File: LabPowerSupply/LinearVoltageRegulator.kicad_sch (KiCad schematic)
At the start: 17 parts, among them Q1_LVR1 PJA3404_R1_00001, Q2_LVR1 PJA3404_R1_00001, Q3_LVR1 PJA3404_R1_00001

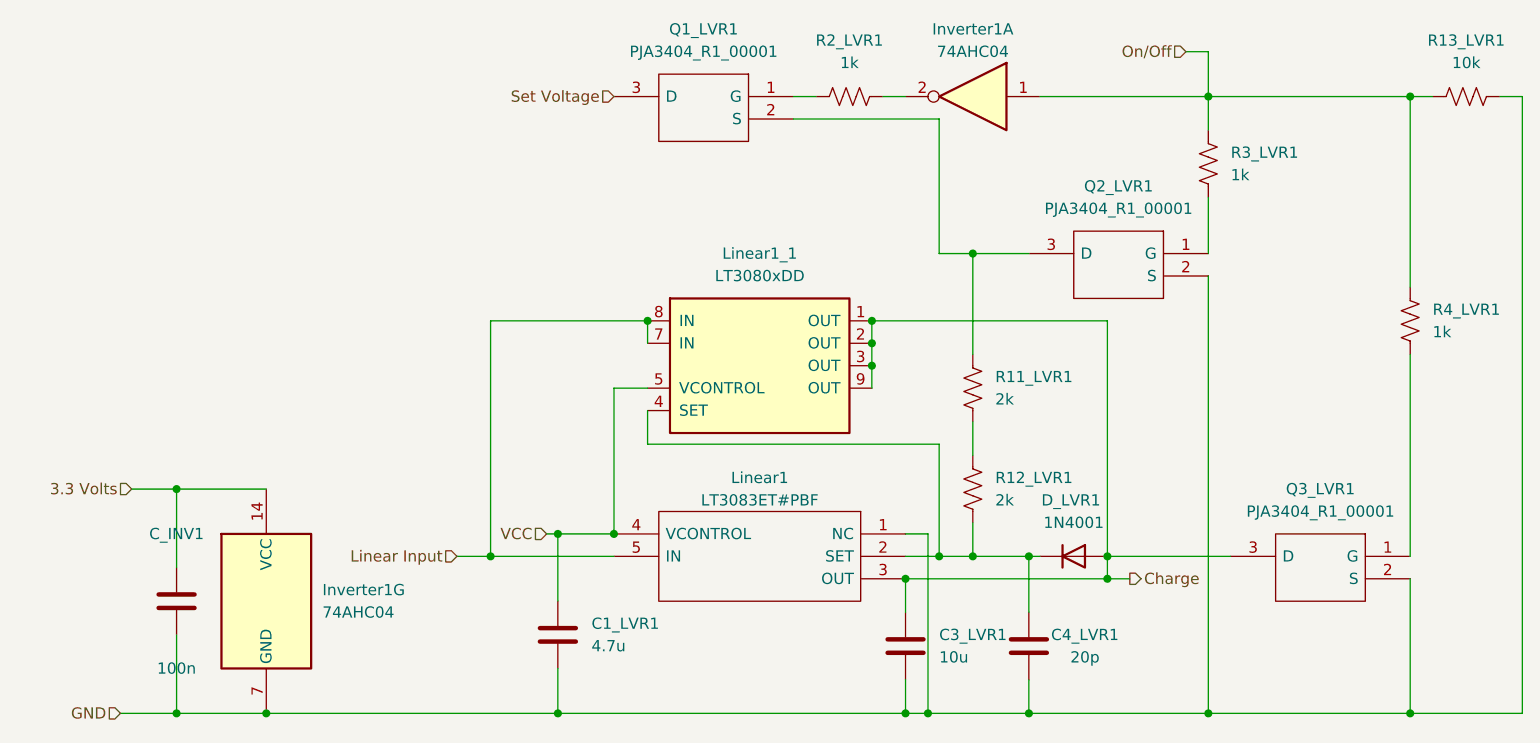
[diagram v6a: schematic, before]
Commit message: Updated Part List
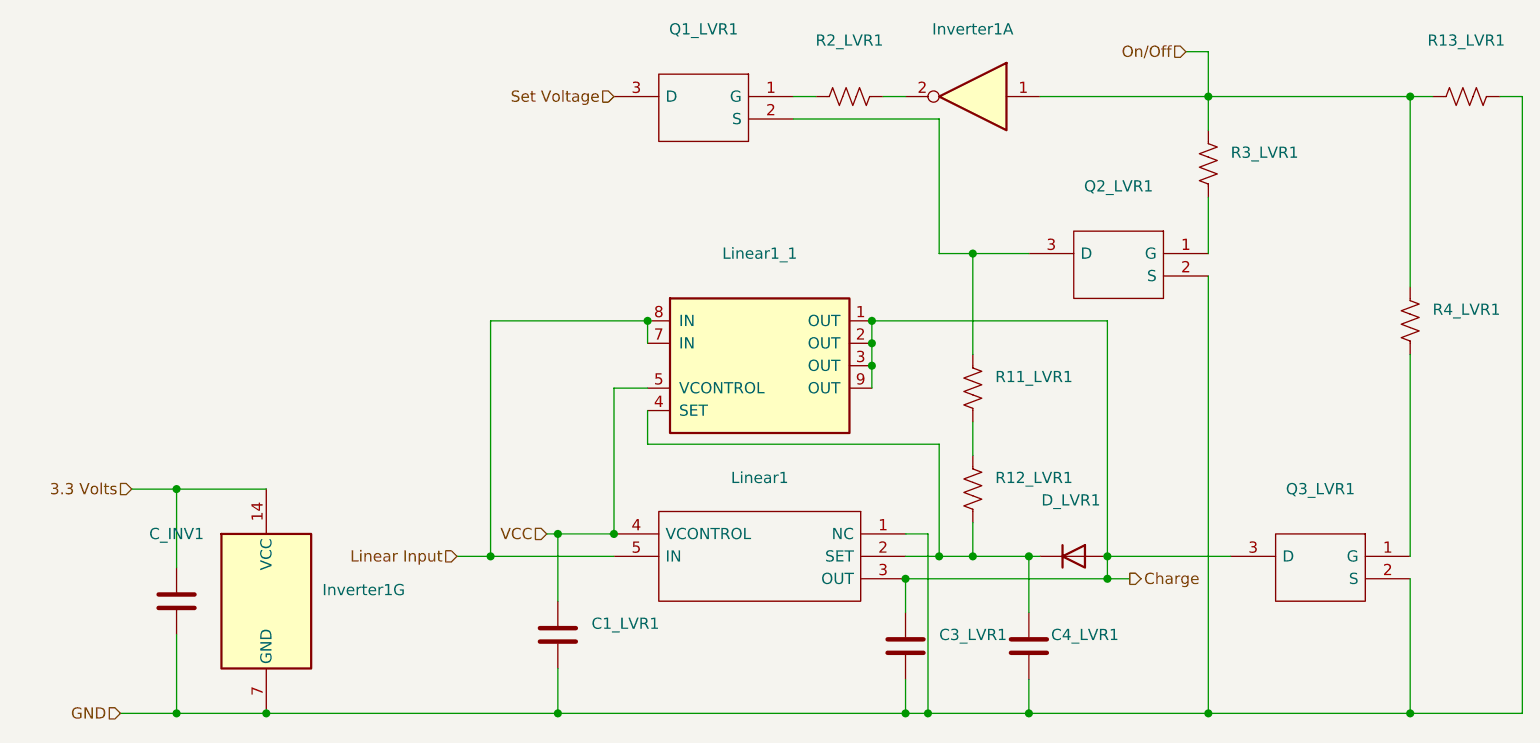
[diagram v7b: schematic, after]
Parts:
- C1_LVR1: value 4.7u -> (none); footprint Capacitor_SMD:C_0805_2012Metric -> (none)
- C3_LVR1: value 10u -> (none); footprint Capacitor_SMD:C_1206_3216Metric -> (none)
- C4_LVR1: value 20p -> (none); footprint Capacitor_SMD:C_0603_1608Metric -> (none)
- C_INV1: value 100n -> (none); footprint Capacitor_SMD:C_0603_1608Metric -> (none)
- D_LVR1: value 1N4001 -> (none); footprint Diode_SMD:D_SMA -> (none)
- Inverter1: value 74AHC04 -> (none); footprint Package_SO:SSOP-14_5.3x6.2mm_P0.65mm -> (none)
- Linear1: value LT3083ET#PBF -> (none); footprint SamacSys_Parts:TO170P457X1022X2306-5P -> (none)
- Linear1_1: value LT3080xDD -> (none); footprint Package_DFN_QFN:DFN-8-1EP_3x3mm_P0.5mm_EP1.66x2.38mm -> (none)
- Q1_LVR1, Q2_LVR1, Q3_LVR1: value PJA3404_R1_00001 -> (none); footprint SamacSys_Parts:SOT95P240X110-3N -> (none)
- R11_LVR1, R12_LVR1: value 2k -> (none); footprint Resistor_SMD:R_0603_1608Metric -> (none)
- R13_LVR1: value 10k -> (none); footprint Resistor_SMD:R_0603_1608Metric -> (none)
- R2_LVR1, R3_LVR1, R4_LVR1: value 1k -> (none); footprint Resistor_SMD:R_0603_1608Metric -> (none)
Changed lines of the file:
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@@
       (effects (font (size 1.27 1.27)) (justify right))
     )
-    (property "Value" "2k" (id 1) (at 180.34 115.5699 0)
-      (effects (font (size 1.27 1.27)) (justify right))
-    )
-    (property "Footprint" "Resistor_SMD:R_0603_1608Metric" (id 2) (at 176.784 114.046 90)
+    (property "Value" "" (id 1) (at 180.34 115.5699 0)
+      (effects (font (size 1.27 1.27)) (justify right))
+    )
+    (property "Footprint" "" (id 2) (at 176.784 114.046 90)
       (effects (font (size 1.27 1.27)) hide)
     )
@@
       (effects (font (size 1.27 1.27)) (justify left))
     )
-    (property "Value" "74AHC04" (id 1) (at 104.14 128.2699 0)
+    (property "Value" "" (id 1) (at 104.14 128.2699 0)
       (effects (font (size 1.27 1.27)) (justify left))
     )
-    (property "Footprint" "Package_SO:SSOP-14_5.3x6.2mm_P0.65mm" (id 2) (at 97.79 127 0)
+    (property "Footprint" "" (id 2) (at 97.79 127 0)
       (effects (font (size 1.27 1.27)) hide)
     )
@@
     (in_bom yes) (on_board yes)
     (property "Reference" "C4_LVR1" (id 0) (at 190.5 130.81 0))
-    (property "Value" "20p" (id 1) (at 190.5 133.35 0))
-    (property "Footprint" "Capacitor_SMD:C_0603_1608Metric" (id 2) (at 185.1152 135.89 0)
+    (property "Value" "" (id 1) (at 190.5 133.35 0))
+    (property "Footprint" "" (id 2) (at 185.1152 135.89 0)
       (effects (font (size 1.27 1.27)) hide)
     )
@@
     (in_bom yes) (on_board yes) (fields_autoplaced)
     (property "Reference" "R2_LVR1" (id 0) (at 163.83 63.5 90))
-    (property "Value" "1k" (id 1) (at 163.83 66.04 90))
-    (property "Footprint" "Resistor_SMD:R_0603_1608Metric" (id 2) (at 164.084 68.834 90)
+    (property "Value" "" (id 1) (at 163.83 66.04 90))
+    (property "Footprint" "" (id 2) (at 164.084 68.834 90)
       (effects (font (size 1.27 1.27)) hide)
     )
@@
       (effects (font (size 1.27 1.27)) (justify right))
     )
-    (property "Value" "2k" (id 1) (at 180.34 104.1399 0)
-      (effects (font (size 1.27 1.27)) (justify right))
-    )
-    (property "Footprint" "Resistor_SMD:R_0603_1608Metric" (id 2) (at 176.784 102.616 90)
+    (property "Value" "" (id 1) (at 180.34 104.1399 0)
+      (effects (font (size 1.27 1.27)) (justify right))
+    )
+    (property "Footprint" "" (id 2) (at 176.784 102.616 90)
       (effects (font (size 1.27 1.27)) hide)
     )
@@
     (in_bom yes) (on_board yes)
     (property "Reference" "Linear1" (id 0) (at 153.67 113.03 0))
-    (property "Value" "LT3083ET#PBF" (id 1) (at 153.67 115.57 0))
-    (property "Footprint" "SamacSys_Parts:TO170P457X1022X2306-5P" (id 2) (at 199.39 116.84 0)
+    (property "Value" "" (id 1) (at 153.67 115.57 0))
+    (property "Footprint" "" (id 2) (at 199.39 116.84 0)
       (effects (font (size 1.27 1.27)) (justify left) hide)
     )
@@
       (effects (font (size 1.27 1.27)) (justify right))
     )
-    (property "Value" "4.7u" (id 1) (at 134.62 132.0799 0)
-      (effects (font (size 1.27 1.27)) (justify right))
-    )
-    (property "Footprint" "Capacitor_SMD:C_0805_2012Metric" (id 2) (at 129.8448 127 0)
+    (property "Value" "" (id 1) (at 134.62 132.0799 0)
+      (effects (font (size 1.27 1.27)) (justify right))
+    )
+    (property "Footprint" "" (id 2) (at 129.8448 127 0)
       (effects (font (size 1.27 1.27)) hide)
     )
@@
     (in_bom yes) (on_board yes) (fields_autoplaced)
     (property "Reference" "Q2_LVR1" (id 0) (at 194.31 80.01 0))
-    (property "Value" "PJA3404_R1_00001" (id 1) (at 194.31 82.55 0))
-    (property "Footprint" "SamacSys_Parts:SOT95P240X110-3N" (id 2) (at 187.96 85.09 0)
+    (property "Value" "" (id 1) (at 194.31 82.55 0))
+    (property "Footprint" "" (id 2) (at 187.96 85.09 0)
       (effects (font (size 1.27 1.27)) (justify left) hide)
     )
@@
     (in_bom yes) (on_board yes) (fields_autoplaced)
     (property "Reference" "Q3_LVR1" (id 0) (at 217.17 114.3 0))
-    (property "Value" "PJA3404_R1_00001" (id 1) (at 217.17 116.84 0))
-    (property "Footprint" "SamacSys_Parts:SOT95P240X110-3N" (id 2) (at 210.82 119.38 0)
+    (property "Value" "" (id 1) (at 217.17 116.84 0))
+    (property "Footprint" "" (id 2) (at 210.82 119.38 0)
       (effects (font (size 1.27 1.27)) (justify left) hide)
     )
@@
       (effects (font (size 1.27 1.27)) (justify right))
     )
-    (property "Value" "1k" (id 1) (at 229.87 96.5199 0)
-      (effects (font (size 1.27 1.27)) (justify right))
-    )
-    (property "Footprint" "Resistor_SMD:R_0603_1608Metric" (id 2) (at 226.314 94.996 90)
+    (property "Value" "" (id 1) (at 229.87 96.5199 0)
+      (effects (font (size 1.27 1.27)) (justify right))
+    )
+    (property "Footprint" "" (id 2) (at 226.314 94.996 90)
       (effects (font (size 1.27 1.27)) hide)
     )
@@
     (in_bom yes) (on_board yes)
     (property "Reference" "Linear1_1" (id 0) (at 153.67 87.63 0))
-    (property "Value" "LT3080xDD" (id 1) (at 153.67 90.17 0))
-    (property "Footprint" "Package_DFN_QFN:DFN-8-1EP_3x3mm_P0.5mm_EP1.66x2.38mm" (id 2) (at 153.67 110.49 0)
+    (property "Value" "" (id 1) (at 153.67 90.17 0))
+    (property "Footprint" "" (id 2) (at 153.67 110.49 0)
       (effects (font (size 1.27 1.27)) hide)
     )
@@
     (in_bom yes) (on_board yes) (fields_autoplaced)
     (property "Reference" "Q1_LVR1" (id 0) (at 147.32 62.23 0))
-    (property "Value" "PJA3404_R1_00001" (id 1) (at 147.32 64.77 0))
-    (property "Footprint" "SamacSys_Parts:SOT95P240X110-3N" (id 2) (at 140.97 67.31 0)
+    (property "Value" "" (id 1) (at 147.32 64.77 0))
+    (property "Footprint" "" (id 2) (at 140.97 67.31 0)
       (effects (font (size 1.27 1.27)) (justify left) hide)
     )
@@
     (in_bom yes) (on_board yes)
     (property "Reference" "D_LVR1" (id 0) (at 188.9125 115.57 0))
-    (property "Value" "1N4001" (id 1) (at 189.23 118.11 0))
-    (property "Footprint" "Diode_SMD:D_SMA" (id 2) (at 189.23 126.365 0)
+    (property "Value" "" (id 1) (at 189.23 118.11 0))
+    (property "Footprint" "" (id 2) (at 189.23 126.365 0)
       (effects (font (size 1.27 1.27)) hide)
     )
@@
     (in_bom yes) (on_board yes)
     (property "Reference" "C_INV1" (id 0) (at 87.63 119.38 0))
-    (property "Value" "100n" (id 1) (at 87.63 134.62 0))
-    (property "Footprint" "Capacitor_SMD:C_0603_1608Metric" (id 2) (at 86.6648 123.19 0)
+    (property "Value" "" (id 1) (at 87.63 134.62 0))
+    (property "Footprint" "" (id 2) (at 86.6648 123.19 0)
       (effects (font (size 1.27 1.27)) hide)
     )
@@
       (effects (font (size 1.27 1.27)) (justify right))
     )
-    (property "Value" "1k" (id 1) (at 207.01 78.7399 0)
-      (effects (font (size 1.27 1.27)) (justify right))
-    )
-    (property "Footprint" "Resistor_SMD:R_0603_1608Metric" (id 2) (at 203.454 77.216 90)
+    (property "Value" "" (id 1) (at 207.01 78.7399 0)
+      (effects (font (size 1.27 1.27)) (justify right))
+    )
+    (property "Footprint" "" (id 2) (at 203.454 77.216 90)
       (effects (font (size 1.27 1.27)) hide)
     )
@@
     (in_bom yes) (on_board yes)
     (property "Reference" "Inverter1" (id 0) (at 177.8 62.23 0))
-    (property "Value" "74AHC04" (id 1) (at 177.8 64.77 0))
-    (property "Footprint" "Package_SO:SSOP-14_5.3x6.2mm_P0.65mm" (id 2) (at 177.8 69.85 0)
+    (property "Value" "" (id 1) (at 177.8 64.77 0))
+    (property "Footprint" "" (id 2) (at 177.8 69.85 0)
       (effects (font (size 1.27 1.27)) hide)
     )
@@
       (effects (font (size 1.27 1.27)) (justify left))
     )
-    (property "Value" "10u" (id 1) (at 173.99 133.3499 0)
+    (property "Value" "" (id 1) (at 173.99 133.3499 0)
       (effects (font (size 1.27 1.27)) (justify left))
     )
-    (property "Footprint" "Capacitor_SMD:C_1206_3216Metric" (id 2) (at 171.1452 135.89 0)
+    (property "Footprint" "" (id 2) (at 171.1452 135.89 0)
       (effects (font (size 1.27 1.27)) hide)
     )
@@
     (in_bom yes) (on_board yes) (fields_autoplaced)
     (property "Reference" "R13_LVR1" (id 0) (at 233.68 63.5 90))
-    (property "Value" "10k" (id 1) (at 233.68 66.04 90))
-    (property "Footprint" "Resistor_SMD:R_0603_1608Metric" (id 2) (at 233.426 70.866 90)
-      (effects (font (size 1.27 1.27)) hide)
-    )
+    (property "Value" "" (id 1) (at 233.68 66.04 90))
+    (property "Footprint" "" (id 2) (at 233.426 70.866 90)
+      (effects (font (size 1.27 1.27)) hide)
+    )
